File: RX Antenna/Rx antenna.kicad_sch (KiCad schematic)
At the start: 11 parts, among them J1 PATCH_FEED, J2 Conn_01x02

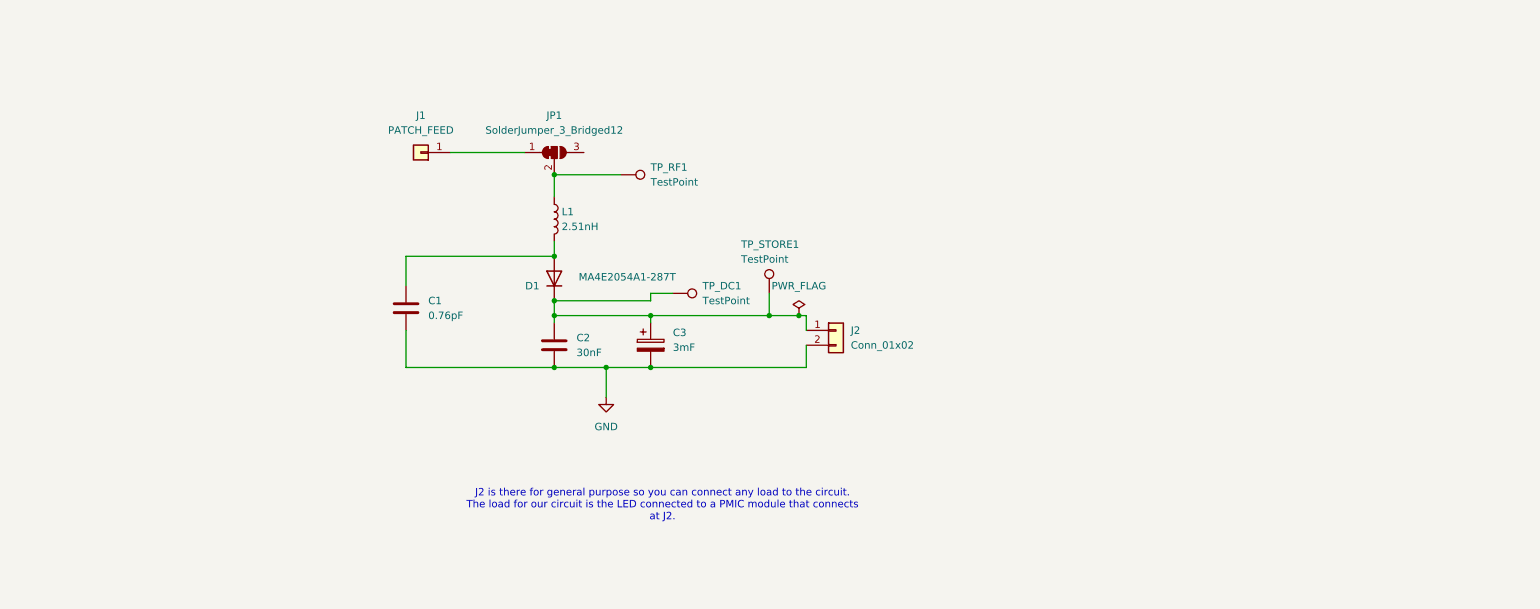
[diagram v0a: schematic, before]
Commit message: rx schematic drawn, need to update values
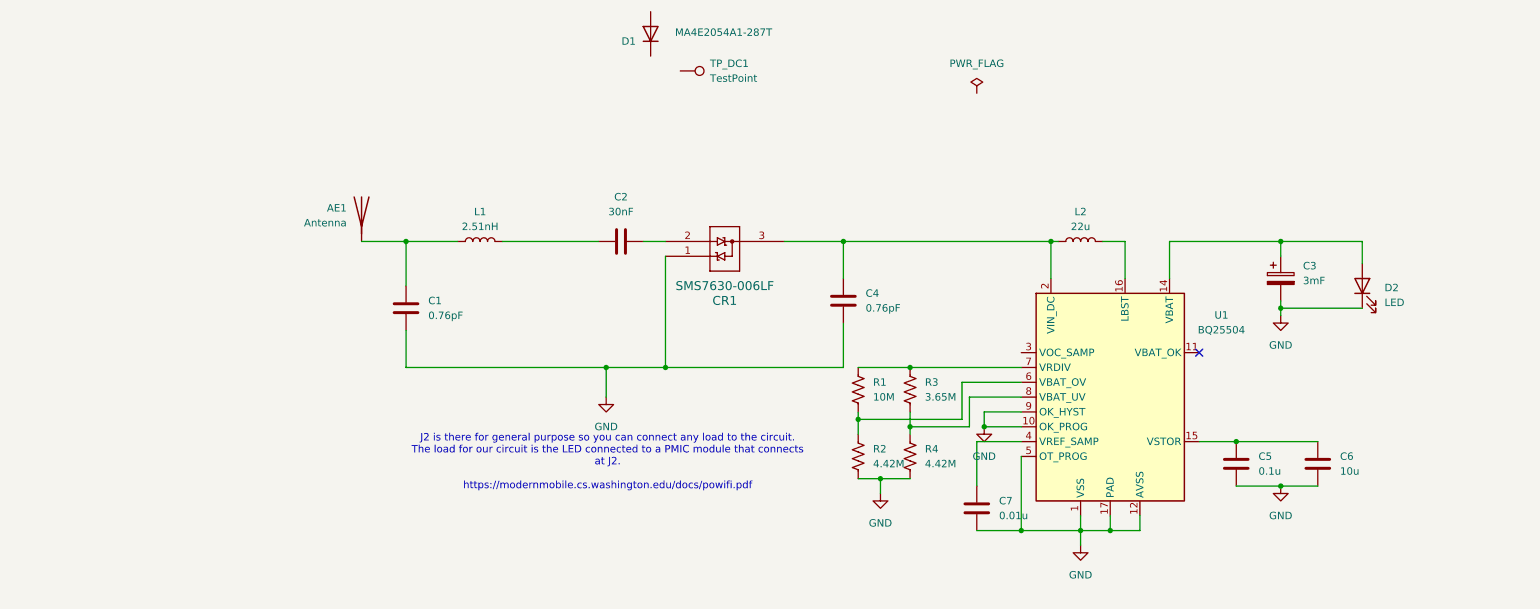
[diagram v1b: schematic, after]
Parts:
- removed J1: PATCH_FEED, Connector_PinHeader_2.54mm:PinHeader_1x01_P2.54mm_Vertical, symbol Connector_Generic:Conn_01x01
- removed J2: Conn_01x02, Connector_PinHeader_2.54mm:PinHeader_1x02_P2.54mm_Vertical, symbol Connector_Generic:Conn_01x02
- removed JP1: SolderJumper_3_Bridged12, Jumper:SolderJumper-3_P1.3mm_Bridged12_RoundedPad1.0x1.5mm, symbol Jumper:SolderJumper_3_Bridged12
- removed TP_RF1, TP_STORE1: TestPoint, TestPoint:TestPoint_Pad_D1.5mm, symbol Connector:TestPoint
- added AE1: Antenna, customFootprints:AperturePatch, symbol Device:Antenna
- added C4: 0.76pF, Capacitor_SMD:C_0402_1005Metric, symbol Device:C
- added C5: 0.1u, Capacitor_SMD:C_0402_1005Metric, symbol Device:C
- added C6: 10u, Capacitor_SMD:C_0402_1005Metric, symbol Device:C
- added C7: 0.01u, Capacitor_SMD:C_0402_1005Metric, symbol Device:C
- added CR1: SMS7630-006LF, Package_TO_SOT_SMD:SOT-23, symbol customSym:SMS7630-006LF
- added D2: LED, symbol Device:LED
- added L2: 22u, Inductor_SMD:L_0402_1005Metric, symbol Device:L
- added R1: 10M, symbol Device:R_US
- added R2, R4: 4.42M, symbol Device:R_US
- added R3: 3.65M, symbol Device:R_US
- added U1: BQ25504, Package_DFN_QFN:VQFN-16-1EP_3x3mm_P0.5mm_EP1.68x1.68mm, symbol Battery_Management:BQ25504
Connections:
- net GND: now also C4.2, C5.2, C6.2, C7.2, CR1.1, D2.1 (K), R2.2, R4.2, U1.1 (VSS), U1.10 (OK_PROG), U1.12 (AVSS), U1.13 (VSS), U1.17 (PAD), U1.5 (OT_PROG), U1.9 (OK_HYST); no longer C2.2
- net at L1.1: now also C1.1, AE1.1 (A)
- new net: C2.1, L1.2
- new net: C2.2, CR1.2
- new net: R1.2, R2.1, U1.6 (VBAT_OV)
- new net: R1.1, R3.1, U1.7 (VRDIV)
- new net: C5.1, C6.1, U1.15 (VSTOR)
- new net: C4.1, CR1.3, L2.1, U1.2 (VIN_DC)
- new net: L2.2, U1.16 (LBST)
- new net: R3.2, R4.1, U1.8 (VBAT_UV)
- new net: C3.1, D2.2 (A), U1.14 (VBAT)
- new net: C7.1, U1.4 (VREF_SAMP)
- now unconnected: D1.1 (K), D1.2 (A), TP_DC1.1
- no-connect marks 0 -> 1
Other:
- note added: "J2 is there for general purpose so you can connect any load to the circuit. The load for our circuit is the LED connected to a PMIC module that connects at J2. https://modernmobile.cs.washington.edu/docs/powifi.pdf"
- note removed: "J2 is there for general purpose so you can connect any load to the circuit. The load for our circuit is the LED connected to a PMIC module that connects at J2."
- moved on the sheet: C2, C3, D1, L1, TP_DC1

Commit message: pcb for rx made
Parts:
- removed D1: MA4E2054A1-287T, Package_TO_SOT_SMD:SOT-23, symbol Device:D
- removed TP_DC1: TestPoint, TestPoint:TestPoint_Pad_D1.5mm, symbol Connector:TestPoint
- added C8: 0.76pF, customFootprints:C_0201_branch, symbol Device:C
- added D3: LED, LED_SMD:LED_0603_1608Metric_Pad1.05x0.95mm_HandSolder, symbol Device:LED
- added J1: Conn_Coaxial, Connector_Coaxial:U.FL_Hirose_U.FL-R-SMT-1_Vertical, symbol Connector:Conn_Coaxial
- added Q1: AO3400A, Package_TO_SOT_SMD:SOT-23, symbol Transistor_FET:AO3400A
- added R10, R11, R12, R8: 0, Resistor_SMD:R_0603_1608Metric_Pad0.98x0.95mm_HandSolder, symbol Device:R_US
- added R5, R6, R7, R9: 10M, Resistor_SMD:R_0603_1608Metric_Pad0.98x0.95mm_HandSolder, symbol Device:R_US
- C1: footprint Capacitor_SMD:C_0402_1005Metric -> Capacitor_SMD:C_0201_0603Metric_Pad0.64x0.40mm_HandSolder
- C2: value 30nF -> 2p; footprint Capacitor_SMD:C_0402_1005Metric -> Capacitor_SMD:C_0201_0603Metric_Pad0.64x0.40mm_HandSolder
- C4: value 0.76pF -> 2p; footprint Capacitor_SMD:C_0402_1005Metric -> Capacitor_SMD:C_0201_0603Metric_Pad0.64x0.40mm_HandSolder
- C5, C6, C7: footprint Capacitor_SMD:C_0402_1005Metric -> Capacitor_SMD:C_0603_1608Metric_Pad1.08x0.95mm_HandSolder
- D2: footprint (none) -> LED_SMD:LED_0603_1608Metric_Pad1.05x0.95mm_HandSolder
- L2: footprint Inductor_SMD:L_0402_1005Metric -> Inductor_SMD:L_1210_3225Metric_Pad1.42x2.65mm_HandSolder
- R1, R2, R3, R4: footprint (none) -> Resistor_SMD:R_0603_1608Metric_Pad0.98x0.95mm_HandSolder
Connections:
- net GND: now also J1.2 (Ext), Q1.2 (S), R10.2, R6.2, R8.2; no longer U1.10 (OK_PROG), U1.9 (OK_HYST)
- net at AE1.1 (A), C1.1, L1.1: now also C8.1
- net at R1.1, R3.1, U1.7 (VRDIV): now also R7.1, R9.1
- net at C4.1, CR1.3, L2.1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: now also R5.1
- net at U1.11 (VBAT_OK): now also Q1.1 (G)
- net at C3.1, U1.14 (VBAT): now also R11.1, R12.1; no longer D2.2 (A)
- net at U1.3 (VOC_SAMP): now also R5.2, R6.1
- new net: C8.2, J1.1 (In)
- new net: R7.2, R8.1, U1.9 (OK_HYST)
- new net: R10.1, R9.2, U1.10 (OK_PROG)
- new net: D3.2 (A), R12.2
- new net: D3.1 (K), Q1.3 (D)
- new net: D2.2 (A), R11.2
- no-connect marks 1 -> 0
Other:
- moved on the sheet: AE1, C1, C2, C4, C5, C6, CR1, D2, L1, R1, R2, R3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

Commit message: updated impedance matching
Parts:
- L1: value 2.51nH -> 2nH; footprint Inductor_SMD:L_0402_1005Metric -> Inductor_SMD:L_0201_0603Metric_Pad0.64x0.40mm_HandSolder
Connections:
- net GND: now also CR1.2; no longer CR1.1
- net at C2.2: now also CR1.3; no longer CR1.2
- net RF_VOUT: now reaches C4.1, L2.1, R5.1, U1.2 (VIN_DC)
- net RF_VOUT: now also CR1.1; no longer CR1.3
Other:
- moved on the sheet: CR1

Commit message: saatvik mad
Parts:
- added C9: 10u, Capacitor_SMD:C_0603_1608Metric_Pad1.08x0.95mm_HandSolder, symbol Device:C
- added JP1: Jumper_2_Open, Jumper:SolderJumper-2_P1.3mm_Open_RoundedPad1.0x1.5mm, symbol Jumper:Jumper_2_Open
- C3: value 3mF -> 100mF
- R1: value 10M -> 7.5M
- R2, R4: value 4.42M -> 7.5M
- R3: value 3.65M -> 2.67M
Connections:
- net GND: now also C9.2
- net RF_VOUT: now also C9.1
- net at AE1.1 (A), C1.1, L1.1: no longer C8.1
- net at C2.1, L1.2: now also C8.1
- net at C5.1, C6.1, U1.15 (VSTOR): now also JP1.1 (A)
- net VOC_SAMP: now reaches R5.2, R6.1, U1.3 (VOC_SAMP)
- net VOC_SAMP: now also JP1.2 (B)
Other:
- moved on the sheet: C8, J1
